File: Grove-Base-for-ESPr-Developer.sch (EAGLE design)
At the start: 8 parts, among them J1 4P-2.0, J2 4P-2.0, J3 4P-2.0, J4 4P-2.0

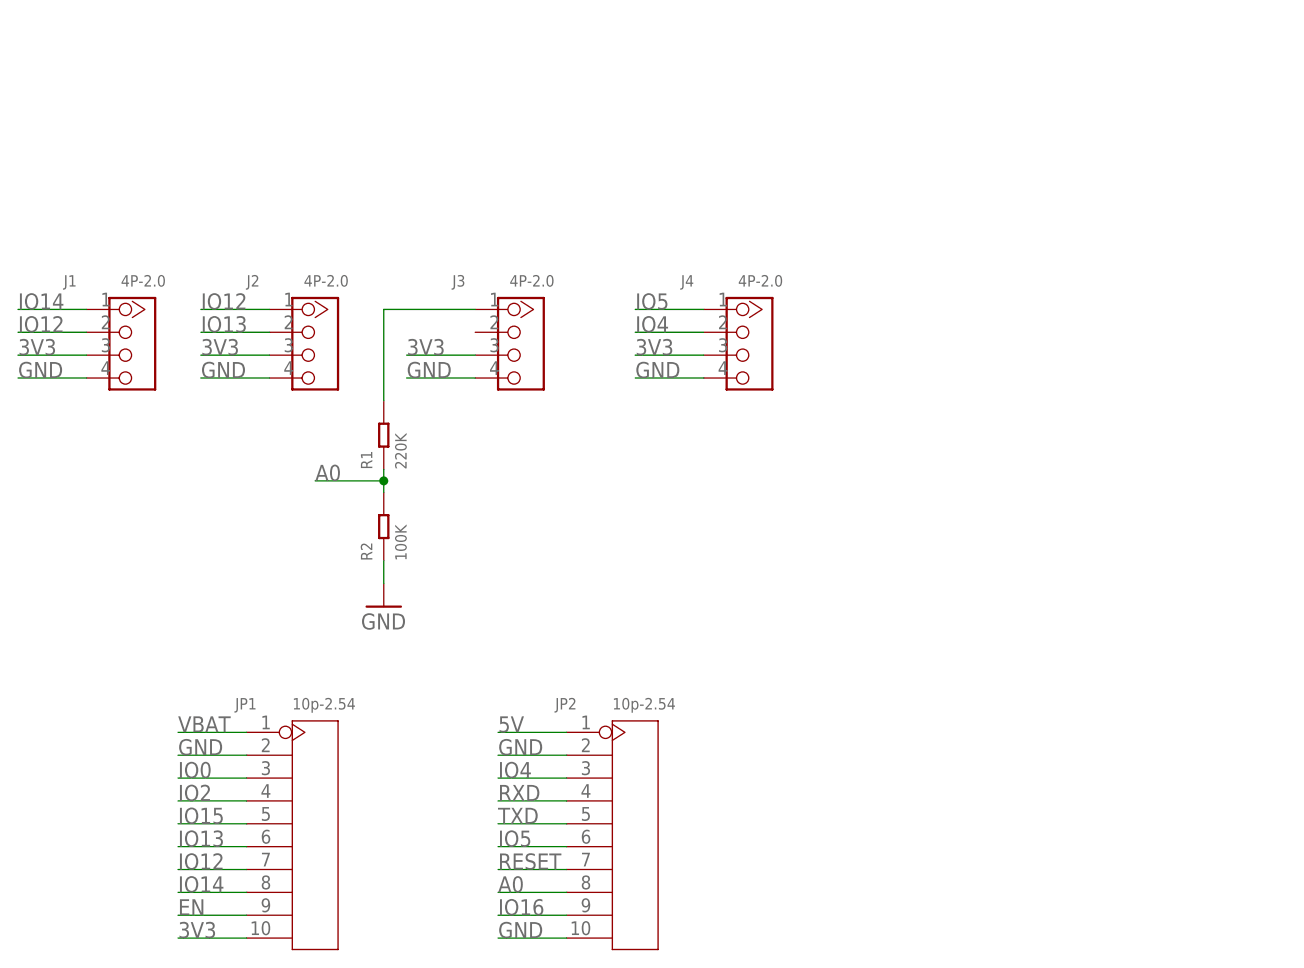
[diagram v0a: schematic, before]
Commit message: Replace the IO14 pin of the IO14 connector with IO15
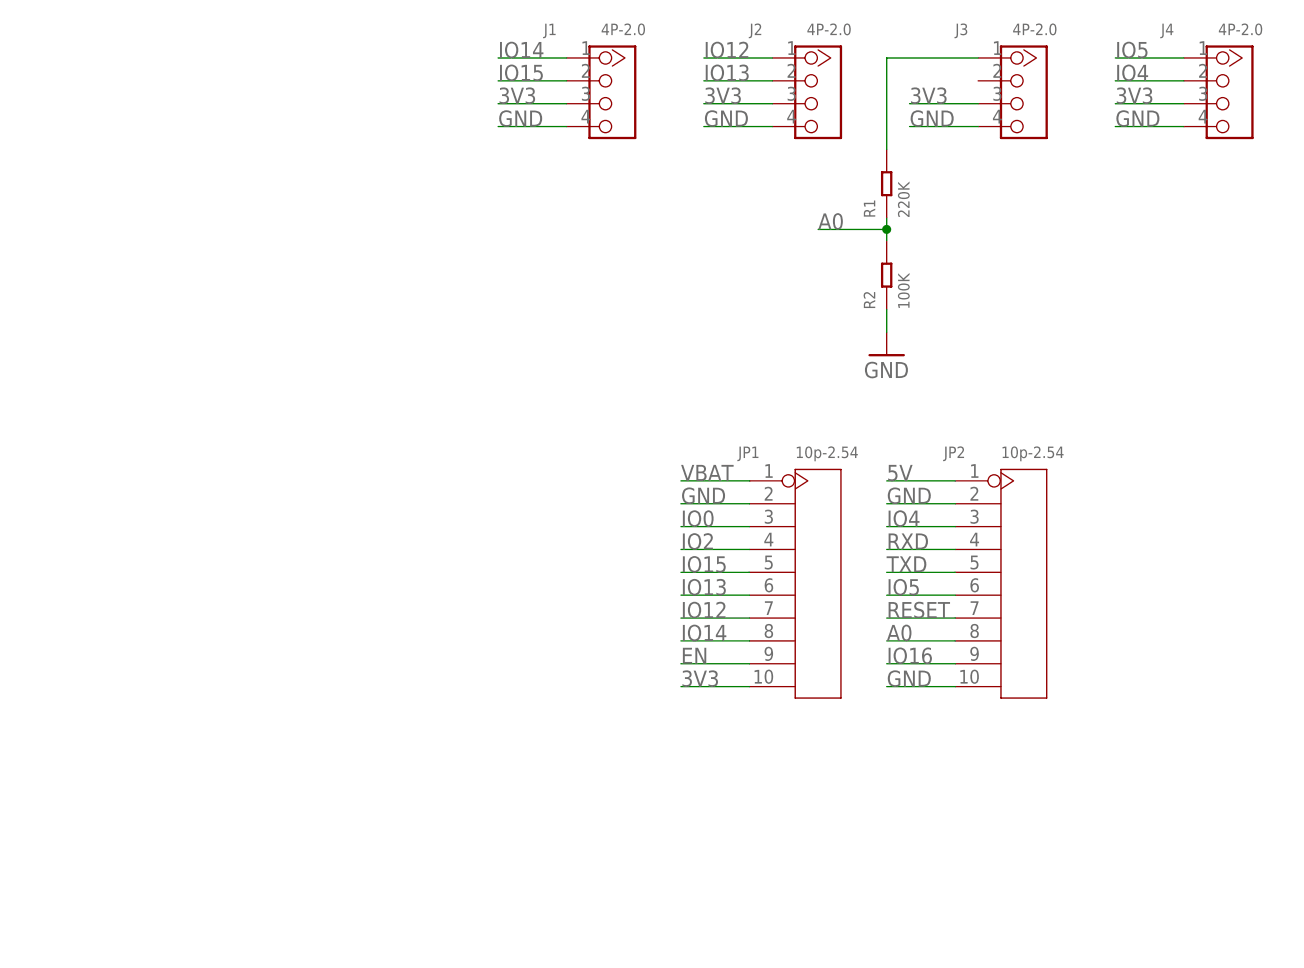
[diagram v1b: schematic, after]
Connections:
- net IO12: no longer J1.2
- net IO15: now also J1.2
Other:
- moved on the sheet: J1, J2, J3, J4, JP1, JP2, R1, R2
